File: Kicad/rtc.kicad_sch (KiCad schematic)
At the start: 6 parts, among them U901 MCP7940N, Y901 32,768 Hz

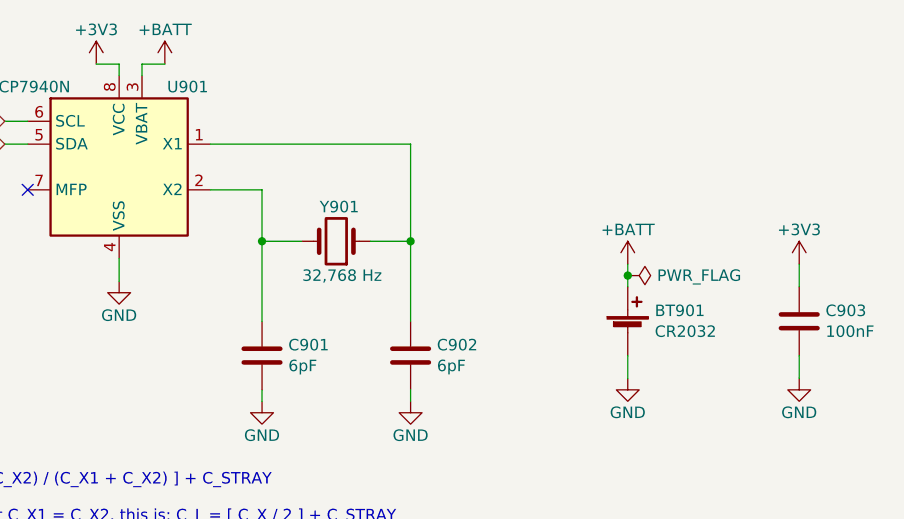
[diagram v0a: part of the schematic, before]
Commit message: Retitle sheets and renumber parts.
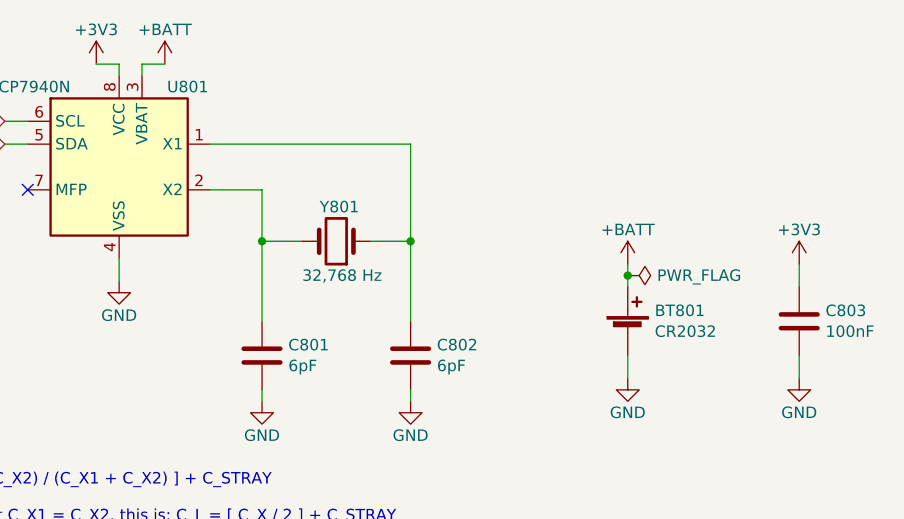
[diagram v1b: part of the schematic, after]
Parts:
- renumbered BT901 to BT801, C901 to C801, C902 to C802, C903 to C803, U901 to U801, Y901 to Y801
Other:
- company: https://neotron-compute.github.io/ -> https://neotron-compute.github.io
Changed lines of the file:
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@@
     (date "${date}")
     (rev "${version}")
-    (company "https://neotron-compute.github.io/")
-    (comment 1 "Licenced as CC BY-SA")
+    (company "https://neotron-compute.github.io")
+    (comment 1 "Licensed as CC-BY-SA")
     (comment 2 "Copyright (c) The Neotron Developers, 2022")
   )
@@
   (symbol (lib_id "power:+3V3") (at 179.07 78.74 0) (unit 1)
     (in_bom yes) (on_board yes)
-    (property "Reference" "#PWR0908" (id 0) (at 179.07 82.55 0)
+    (property "Reference" "#PWR0808" (id 0) (at 179.07 82.55 0)
       (effects (font (size 1.27 1.27)) hide)
     )
@@
   (symbol (lib_id "Device:C") (at 179.07 85.09 0) (unit 1)
     (in_bom yes) (on_board yes)
-    (property "Reference" "C903" (id 0) (at 181.991 83.9216 0)
+    (property "Reference" "C803" (id 0) (at 181.991 83.9216 0)
       (effects (font (size 1.27 1.27)) (justify left))
     )
@@
   (symbol (lib_id "power:GND") (at 179.07 91.44 0) (unit 1)
     (in_bom yes) (on_board yes)
-    (property "Reference" "#PWR0909" (id 0) (at 179.07 97.79 0)
+    (property "Reference" "#PWR0809" (id 0) (at 179.07 97.79 0)
       (effects (font (size 1.27 1.27)) hide)
     )
@@
   (symbol (lib_id "power:+3V3") (at 100.965 56.515 0) (unit 1)
     (in_bom yes) (on_board yes)
-    (property "Reference" "#PWR0901" (id 0) (at 100.965 60.325 0)
+    (property "Reference" "#PWR0801" (id 0) (at 100.965 60.325 0)
       (effects (font (size 1.27 1.27)) hide)
     )
@@
   (symbol (lib_id "power:GND") (at 103.505 80.645 0) (unit 1)
     (in_bom yes) (on_board yes)
-    (property "Reference" "#PWR0902" (id 0) (at 103.505 86.995 0)
+    (property "Reference" "#PWR0802" (id 0) (at 103.505 86.995 0)
       (effects (font (size 1.27 1.27)) hide)
     )
@@
   (symbol (lib_id "Device:Crystal") (at 127.635 76.2 180) (unit 1)
     (in_bom yes) (on_board yes)
-    (property "Reference" "Y901" (id 0) (at 130.175 72.39 0)
+    (property "Reference" "Y801" (id 0) (at 130.175 72.39 0)
       (effects (font (size 1.27 1.27)) (justify left))
     )
@@
   (symbol (lib_id "power:+BATT") (at 108.585 56.515 0) (unit 1)
     (in_bom yes) (on_board yes)
-    (property "Reference" "#PWR0903" (id 0) (at 108.585 60.325 0)
+    (property "Reference" "#PWR0803" (id 0) (at 108.585 60.325 0)
       (effects (font (size 1.27 1.27)) hide)
     )
@@
   (symbol (lib_id "power:+BATT") (at 160.02 78.74 0) (unit 1)
     (in_bom yes) (on_board yes)
-    (property "Reference" "#PWR0906" (id 0) (at 160.02 82.55 0)
+    (property "Reference" "#PWR0806" (id 0) (at 160.02 82.55 0)
       (effects (font (size 1.27 1.27)) hide)
     )
@@
   (symbol (lib_id "power:GND") (at 160.02 91.44 0) (unit 1)
     (in_bom yes) (on_board yes)
-    (property "Reference" "#PWR0907" (id 0) (at 160.02 97.79 0)
+    (property "Reference" "#PWR0807" (id 0) (at 160.02 97.79 0)
       (effects (font (size 1.27 1.27)) hide)
     )
@@
   (symbol (lib_id "Device:C") (at 135.89 88.9 0) (unit 1)
     (in_bom yes) (on_board yes)
-    (property "Reference" "C902" (id 0) (at 138.811 87.7316 0)
+    (property "Reference" "C802" (id 0) (at 138.811 87.7316 0)
       (effects (font (size 1.27 1.27)) (justify left))
     )
@@
   (symbol (lib_id "Device:C") (at 119.38 88.9 0) (unit 1)
     (in_bom yes) (on_board yes)
-    (property "Reference" "C901" (id 0) (at 122.301 87.7316 0)
+    (property "Reference" "C801" (id 0) (at 122.301 87.7316 0)
       (effects (font (size 1.27 1.27)) (justify left))
     )
@@
   (symbol (lib_id "power:GND") (at 119.38 93.98 0) (unit 1)
     (in_bom yes) (on_board yes)
-    (property "Reference" "#PWR0904" (id 0) (at 119.38 100.33 0)
+    (property "Reference" "#PWR0804" (id 0) (at 119.38 100.33 0)
       (effects (font (size 1.27 1.27)) hide)
     )
@@
   (symbol (lib_id "Timer_RTC:MCP7940N-xP") (at 103.505 67.945 0) (unit 1)
     (in_bom yes) (on_board yes)
-    (property "Reference" "U901" (id 0) (at 111.125 59.055 0))
+    (property "Reference" "U801" (id 0) (at 111.125 59.055 0))
     (property "Value" "MCP7940N" (id 1) (at 93.345 59.055 0))
     (property "Footprint" "Package_DIP:DIP-8_W7.62mm" (id 2) (at 103.505 67.945 0)
@@
   (symbol (lib_id "Device:Battery_Cell") (at 160.02 86.36 0) (unit 1)
     (in_bom yes) (on_board yes)
-    (property "Reference" "BT901" (id 0) (at 163.0172 83.9216 0)
+    (property "Reference" "BT801" (id 0) (at 163.0172 83.9216 0)
       (effects (font (size 1.27 1.27)) (justify left))
     )
@@
   (symbol (lib_id "power:PWR_FLAG") (at 160.02 80.01 270) (unit 1)
     (in_bom yes) (on_board yes)
-    (property "Reference" "#FLG0901" (id 0) (at 161.925 80.01 0)
+    (property "Reference" "#FLG0801" (id 0) (at 161.925 80.01 0)
       (effects (font (size 1.27 1.27)) hide)
     )
@@
   (symbol (lib_id "power:GND") (at 135.89 93.98 0) (unit 1)
     (in_bom yes) (on_board yes)
-    (property "Reference" "#PWR0905" (id 0) (at 135.89 100.33 0)
-      (effects (font (size 1.27 1.27)) hide)
-    )
+    (property "Reference" "#PWR0805" (id 0) (at 135.89 100.33 0)
+      (effects (font (size 1.27 1.27)) hide)
+    )

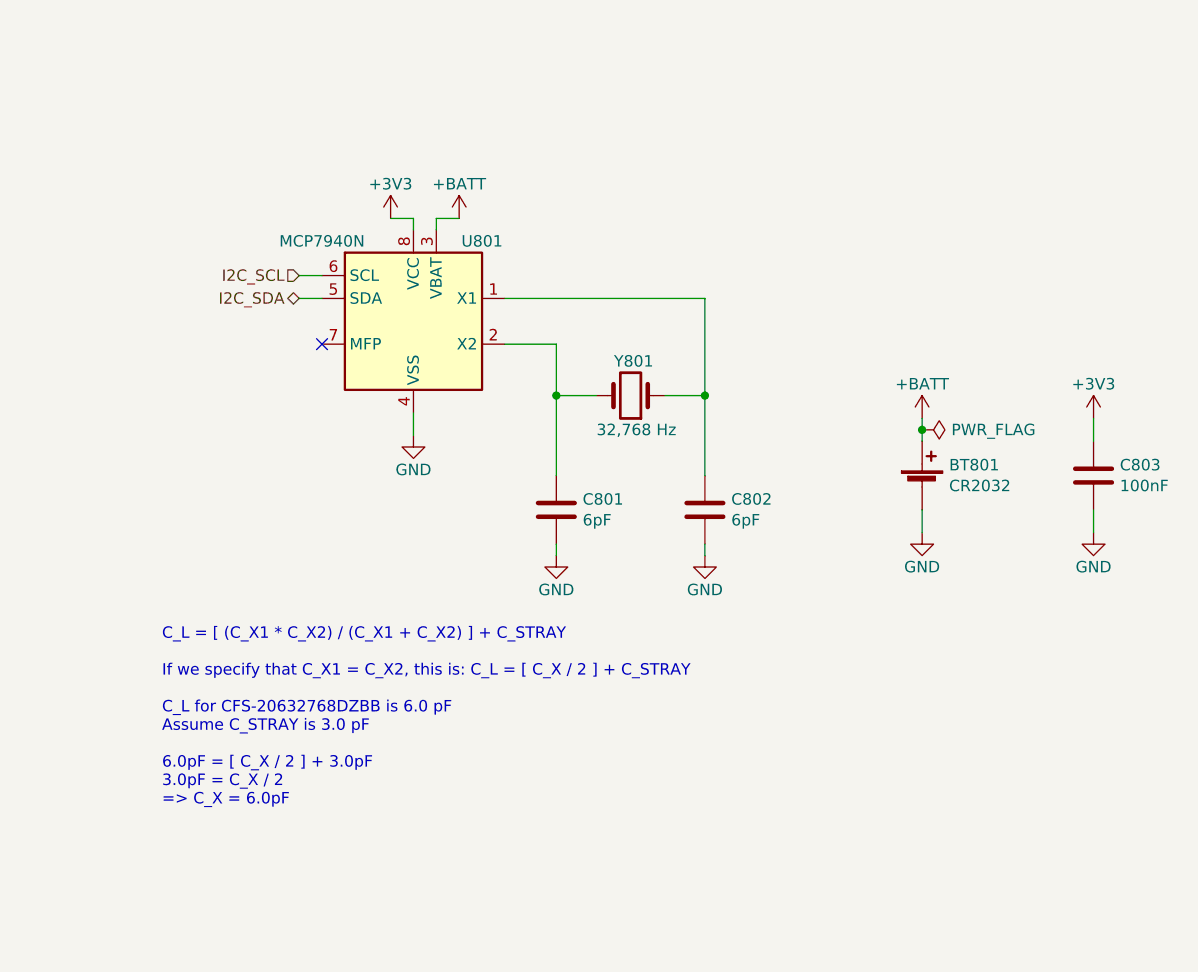
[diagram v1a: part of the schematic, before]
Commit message: Change RTC to DS1307.
It's a SOIC-8 and there's a few other parts that will fit. It also
needs no load capacitors on the crystal.

The PCB change includes a slight tidy-up of the CODEC 3.3V line, and
I moved the SPI lines into the BMC apart.
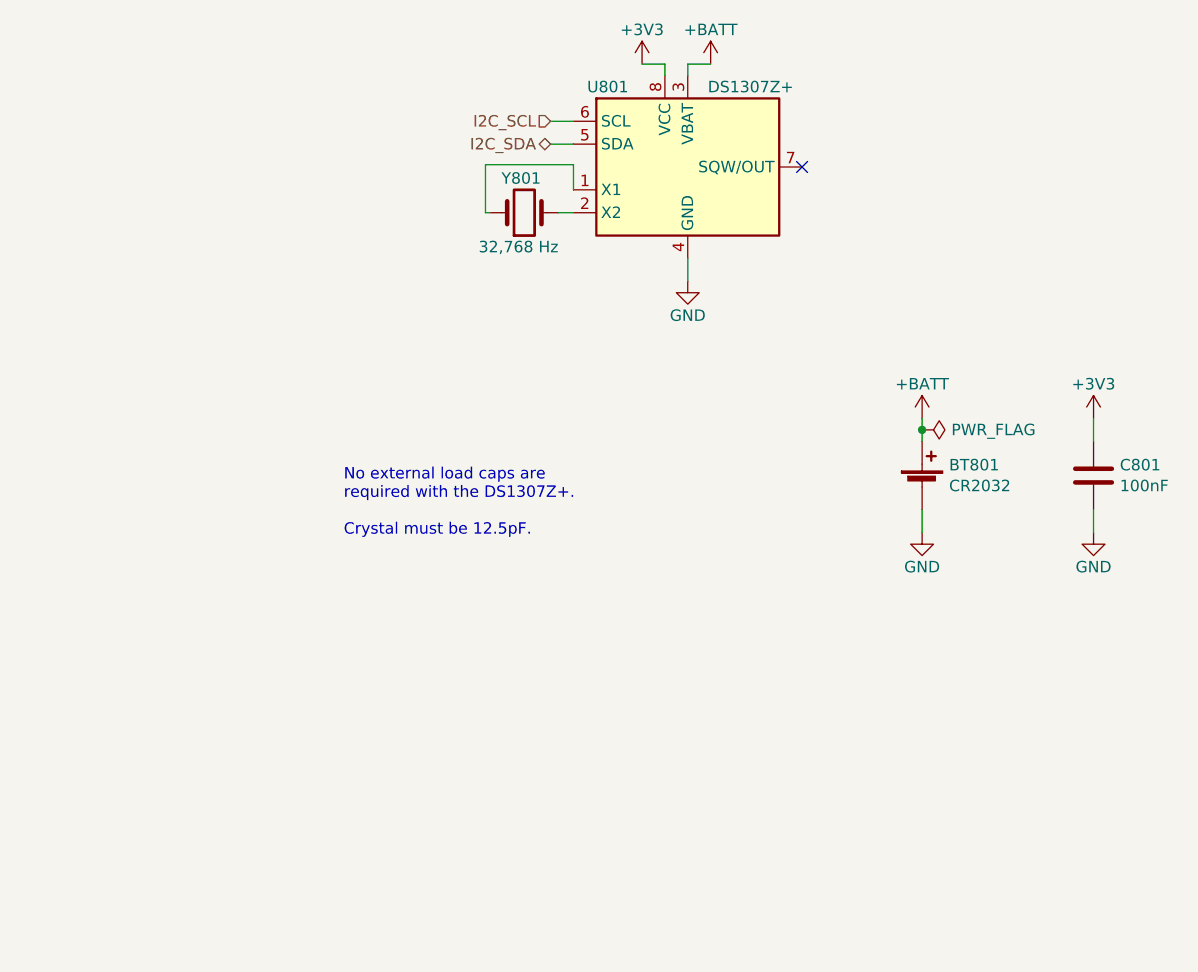
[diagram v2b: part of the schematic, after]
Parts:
- removed C801, C802: 6pF, Capacitor_SMD:C_0805_2012Metric_Pad1.18x1.45mm_HandSolder, symbol Device:C
- removed U801: MCP7940N, Package_DIP:DIP-8_W7.62mm, symbol Timer_RTC:MCP7940N-xP
- added U801: DS1307Z+, Package_SO:SOIC-8_3.9x4.9mm_P1.27mm, symbol Timer_RTC:DS1307Z+
- Y801: footprint Crystal:Crystal_DS26_D2.0mm_L6.0mm_Horizontal -> Crystal:Crystal_SMD_3215-2Pin_3.2x1.5mm; Digikey 300-8301-ND -> SER4103TR-ND; LCSC Part# (none) -> C32346; MPN CFS-20632768DZBB -> FC-135 32.7680KA-A5; Manufacturer Citizen -> Seiko Epson; Mouser CFS-20632768DZBB -> (none)
- renumbered C803 to C801
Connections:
- net +3V3: now also U801.8 (VCC)
- net +BATT: now also U801.3 (VBAT)
- net GND: now also U801.4 (GND)
- net I2C_SCL: now also U801.6 (SCL)
- net I2C_SDA: now also U801.5 (SDA)
- net at Y801.1: now also U801.1 (X1)
- net at Y801.2: now also U801.2 (X2)
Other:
- note added: "No external load caps are required with the DS1307Z+. Crystal must be 12.5pF."
- note removed: "C_L = [ (C_X1 * C_X2) / (C_X1 + C_X2) ] + C_STRAY If we specify that C_X1 = C_X2, this is: C_L = [ C_X / 2 ] + C_STRAY C_L for CFS-20632768DZBB is 6.0 pF Assume C_STRAY is 3.0 pF 6.0pF = [ C_X / 2 ] + 3.0pF 3.0pF = C_X / 2 => C_X = 6.0pF"
- moved on the sheet: Y801

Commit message: Removed all CPL parts, and changed standby PSU.
The Holtek was a SOT-89 that had a completely different pinout to
every other SOT-89 3.3V LDO out there. To avoid confusion I
wanted to replace it, but the only other basic JLCPCB parts
were the AMS1117 (huge quiescent current) and something only
rated to 7V input voltage (this LDO gets the full VDC in).

So, I used a TO-92 footprint and picked an LP2950N.

This, however, needs some ESR on the output cap, so I made
that a 2.2uF electrolytic.

I also removed the 2x 10uF output caps on the K7805 and set
just one 22uF as specified in the datasheet.
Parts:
- C801: Digikey (none) -> 399-C0805C104M5RAC7800CT-ND; MPN CPL-CAP-X7R-0805-100NF-50V -> C0805C104M5RACTU; Manufacturer CPL -> Kemet; Mouser (none) -> 80-C0805C104M5R
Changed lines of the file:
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@@
       (effects (font (size 1.27 1.27)) hide)
     )
-    (property "Manufacturer" "CPL" (id 4) (at 0 170.18 0)
+    (property "Manufacturer" "Kemet" (id 4) (at 0 170.18 0)
       (effects (font (size 1.27 1.27)) hide)
     )
@@
       (effects (font (size 1.27 1.27)) hide)
     )
-    (property "Digikey" "~" (id 6) (at 179.07 85.09 0)
+    (property "Digikey" "399-C0805C104M5RAC7800CT-ND" (id 6) (at 179.07 85.09 0)
       (effects (font (size 1.27 1.27)) hide)
     )
-    (property "MPN" "CPL-CAP-X7R-0805-100NF-50V" (id 7) (at 179.07 85.09 0)
+    (property "MPN" "C0805C104M5RACTU" (id 7) (at 179.07 85.09 0)
       (effects (font (size 1.27 1.27)) hide)
     )
-    (property "Mouser" "~" (id 8) (at 179.07 85.09 0)
+    (property "Mouser" "80-C0805C104M5R" (id 8) (at 179.07 85.09 0)
       (effects (font (size 1.27 1.27)) hide)
     )

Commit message: Swap to an Adam Tech battery holder.
Pretty sure it'll just fit on the Keystone 103 footprint so
I didn't change it.
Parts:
- BT801: Digikey 36-103-ND -> 2057-BH-80A-1-ND; MPN 103 -> BH-80A-1; Manufacturer Keystone -> Adam Tech
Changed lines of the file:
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@@
       (effects (font (size 1.27 1.27)) hide)
     )
-    (property "Datasheet" "http://keyelco.com/userAssets/file/M65p3.pdf" (id 3) (at 160.02 84.836 90)
+    (property "Datasheet" "https://app.adam-tech.com/products/download/data_sheet/197029/bh-80a-1-data-sheet.pdf" (id 3) (at 160.02 84.836 90)
       (effects (font (size 1.27 1.27)) hide)
     )
-    (property "Manufacturer" "Keystone" (id 4) (at 160.02 86.36 0)
+    (property "Manufacturer" "Adam Tech" (id 4) (at 160.02 86.36 0)
       (effects (font (size 1.27 1.27)) hide)
     )
@@
       (effects (font (size 1.27 1.27)) hide)
     )
-    (property "MPN" "103" (id 6) (at 160.02 86.36 0)
+    (property "MPN" "BH-80A-1" (id 6) (at 160.02 86.36 0)
       (effects (font (size 1.27 1.27)) hide)
     )
-    (property "Digikey" "36-103-ND" (id 7) (at 160.02 86.36 0)
+    (property "Digikey" "2057-BH-80A-1-ND" (id 7) (at 160.02 86.36 0)
       (effects (font (size 1.27 1.27)) hide)
     )
